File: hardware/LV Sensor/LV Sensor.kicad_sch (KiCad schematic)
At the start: 75 parts, among them J1 Conn_01x04_Pin, J2 Conn_01x02_Pin, J3 TH, J4 TH, J5 TH, J6 TH, SW1 SW_Push, U1 MSPM0G3507 RHB32, U10 DXTN80100CFGQ, U2 ISO1042BDW, U3 KA78M05_TO252, U4 KA78M05_TO252, U5 L78L33_SO8, U6 LM324BAIPWR, U7 HBDM60V600X, U8 LM324BAIPWR, U9 DXTN80100CFGQ

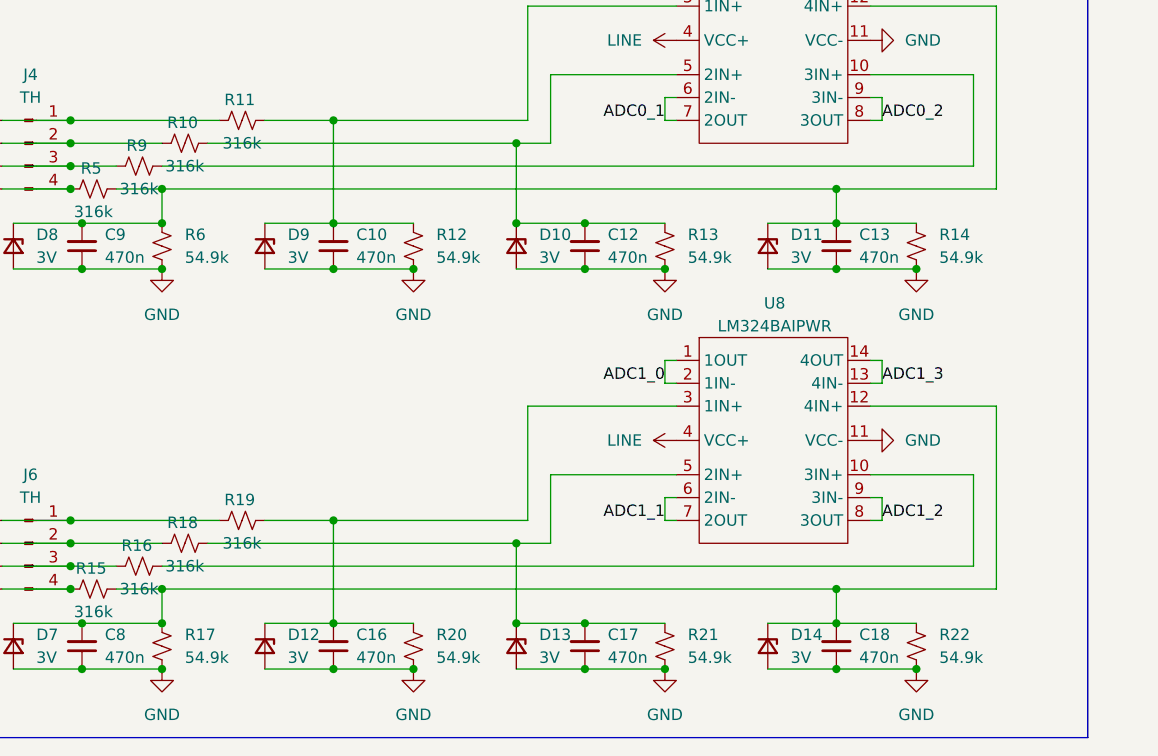
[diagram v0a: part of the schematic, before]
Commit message: miswired filter, also forgot about negative ranges
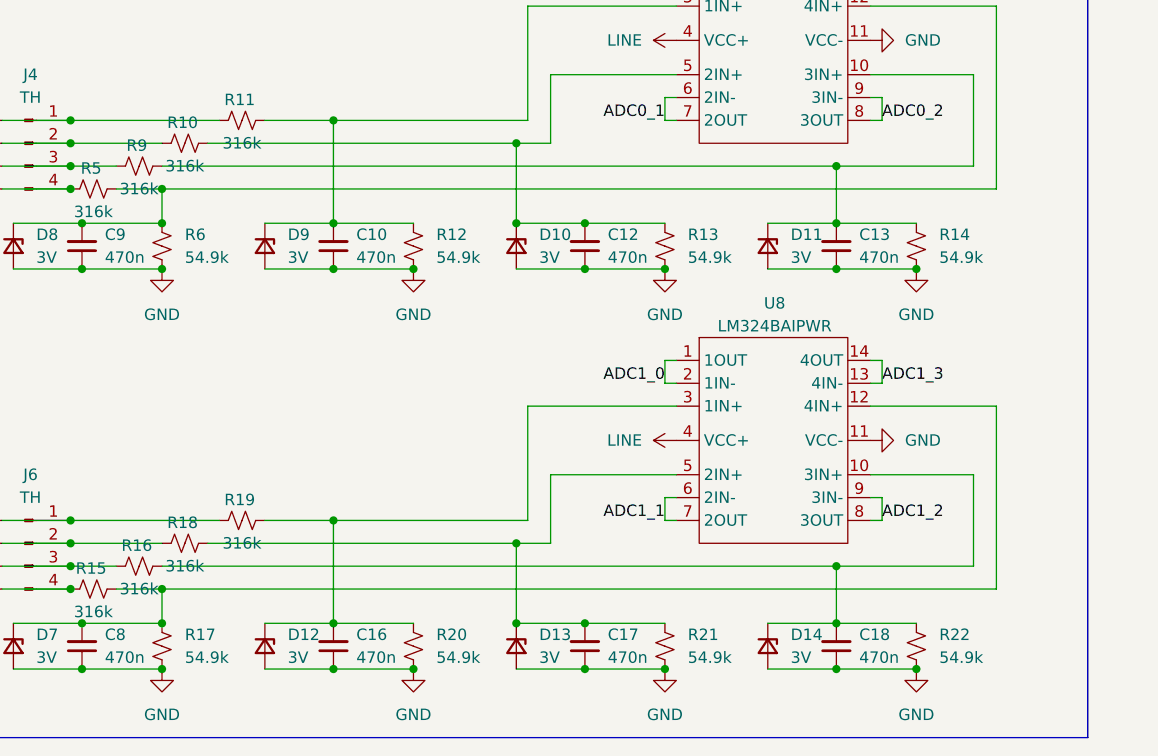
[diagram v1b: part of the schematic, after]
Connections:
- net at C9.2, D8.1 (K), R5.2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: no longer C13.2, D11.1 (K), R14.2
- net at C8.2, D7.1 (K), R15.2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: no longer C18.2, D14.1 (K), R22.2
- net at R9.2, U6.10 (3IN+): now also C13.2, D11.1 (K), R14.2
- net at R16.2, U8.10 (3IN+): now also C18.2, D14.1 (K), R22.2
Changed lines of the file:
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@@
-	)
-	(junction
-		(at 115.57 180.34)
-		(diameter 0)
-		(color 0 0 0 0)
 	)
 	(junction
@@
 	)
 	(junction
-		(at 115.57 135.89)
-		(diameter 0)
-		(color 0 0 0 0)
-	)
-	(junction
 		(at 106.68 86.36)
 		(diameter 0)
@@
 	)
 	(junction
+		(at 115.57 133.35)
+		(diameter 0)
+		(color 0 0 0 0)
+	)
+	(junction
 		(at 59.69 189.23)
 		(diameter 0)
@@
 	(junction
 		(at 87.63 41.91)
+		(diameter 0)
+		(color 0 0 0 0)
+	)
+	(junction
+		(at 115.57 177.8)
 		(diameter 0)
 		(color 0 0 0 0)
@@
 	(wire
 		(pts
-			(xy 115.57 135.89) (xy 133.35 135.89)
+			(xy 40.64 135.89) (xy 133.35 135.89)
 		)
 		(stroke
@@
 	(wire
 		(pts
+			(xy 115.57 177.8) (xy 115.57 184.15)
+		)
+		(stroke
+			(width 0)
+			(type default)
+		)
+	)
+	(wire
+		(pts
 			(xy 39.37 36.83) (xy 46.99 36.83)
 		)
@@
 	(wire
 		(pts
-			(xy 40.64 177.8) (xy 130.81 177.8)
+			(xy 40.64 177.8) (xy 115.57 177.8)
 		)
 		(stroke
@@
 	(wire
 		(pts
-			(xy 115.57 180.34) (xy 115.57 184.15)
-		)
-		(stroke
-			(width 0)
-			(type default)
-		)
-	)
-	(wire
-		(pts
 			(xy 120.65 154.94) (xy 119.38 154.94)
 		)
@@
 	(wire
 		(pts
-			(xy 40.64 133.35) (xy 130.81 133.35)
+			(xy 40.64 133.35) (xy 115.57 133.35)
 		)
 		(stroke
@@
 	(wire
 		(pts
+			(xy 115.57 133.35) (xy 115.57 139.7)
+		)
+		(stroke
+			(width 0)
+			(type default)
+		)
+	)
+	(wire
+		(pts
 			(xy 22.86 81.28) (xy 22.86 93.98)
 		)
@@
 	(wire
 		(pts
+			(xy 115.57 177.8) (xy 130.81 177.8)
+		)
+		(stroke
+			(width 0)
+			(type default)
+		)
+	)
+	(wire
+		(pts
 			(xy 69.85 49.53) (xy 80.01 49.53)
 		)
@@
 	(wire
 		(pts
+			(xy 115.57 133.35) (xy 130.81 133.35)
+		)
+		(stroke
+			(width 0)
+			(type default)
+		)
+	)
+	(wire
+		(pts
 			(xy 191.77 49.53) (xy 201.93 49.53)
 		)
@@
 	(wire
 		(pts
-			(xy 40.64 135.89) (xy 115.57 135.89)
-		)
-		(stroke
-			(width 0)
-			(type default)
-		)
-	)
-	(wire
-		(pts
 			(xy 22.86 135.89) (xy 30.48 135.89)
 		)
@@
 	(wire
 		(pts
-			(xy 40.64 180.34) (xy 115.57 180.34)
+			(xy 40.64 180.34) (xy 133.35 180.34)
 		)
 		(stroke
@@
 	(wire
 		(pts
-			(xy 115.57 135.89) (xy 115.57 139.7)
-		)
-		(stroke
-			(width 0)
-			(type default)
-		)
-	)
-	(wire
-		(pts
 			(xy 133.35 41.91) (xy 132.08 41.91)
 		)
@@
 		)
 		(stroke
-			(width 0)
-			(type default)
-		)
-	)
-	(wire
-		(pts
-			(xy 115.57 180.34) (xy 133.35 180.34)
-		)
-		(stroke

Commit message: asd
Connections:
- net LED_GREEN: no longer U1.27 (PA23_VREF+)
- net LED_RED_N: no longer U1.26 (PA22_A0_7)
- no-connect marks 8 -> 6
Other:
- note added: "TODO. somehow support negative voltage range, like 2 inputs that support it, the rest can get shoved thoruhg the ADC's. probably a external adc IC"
- moved on the sheet: D5, D6, R3, R4, U7

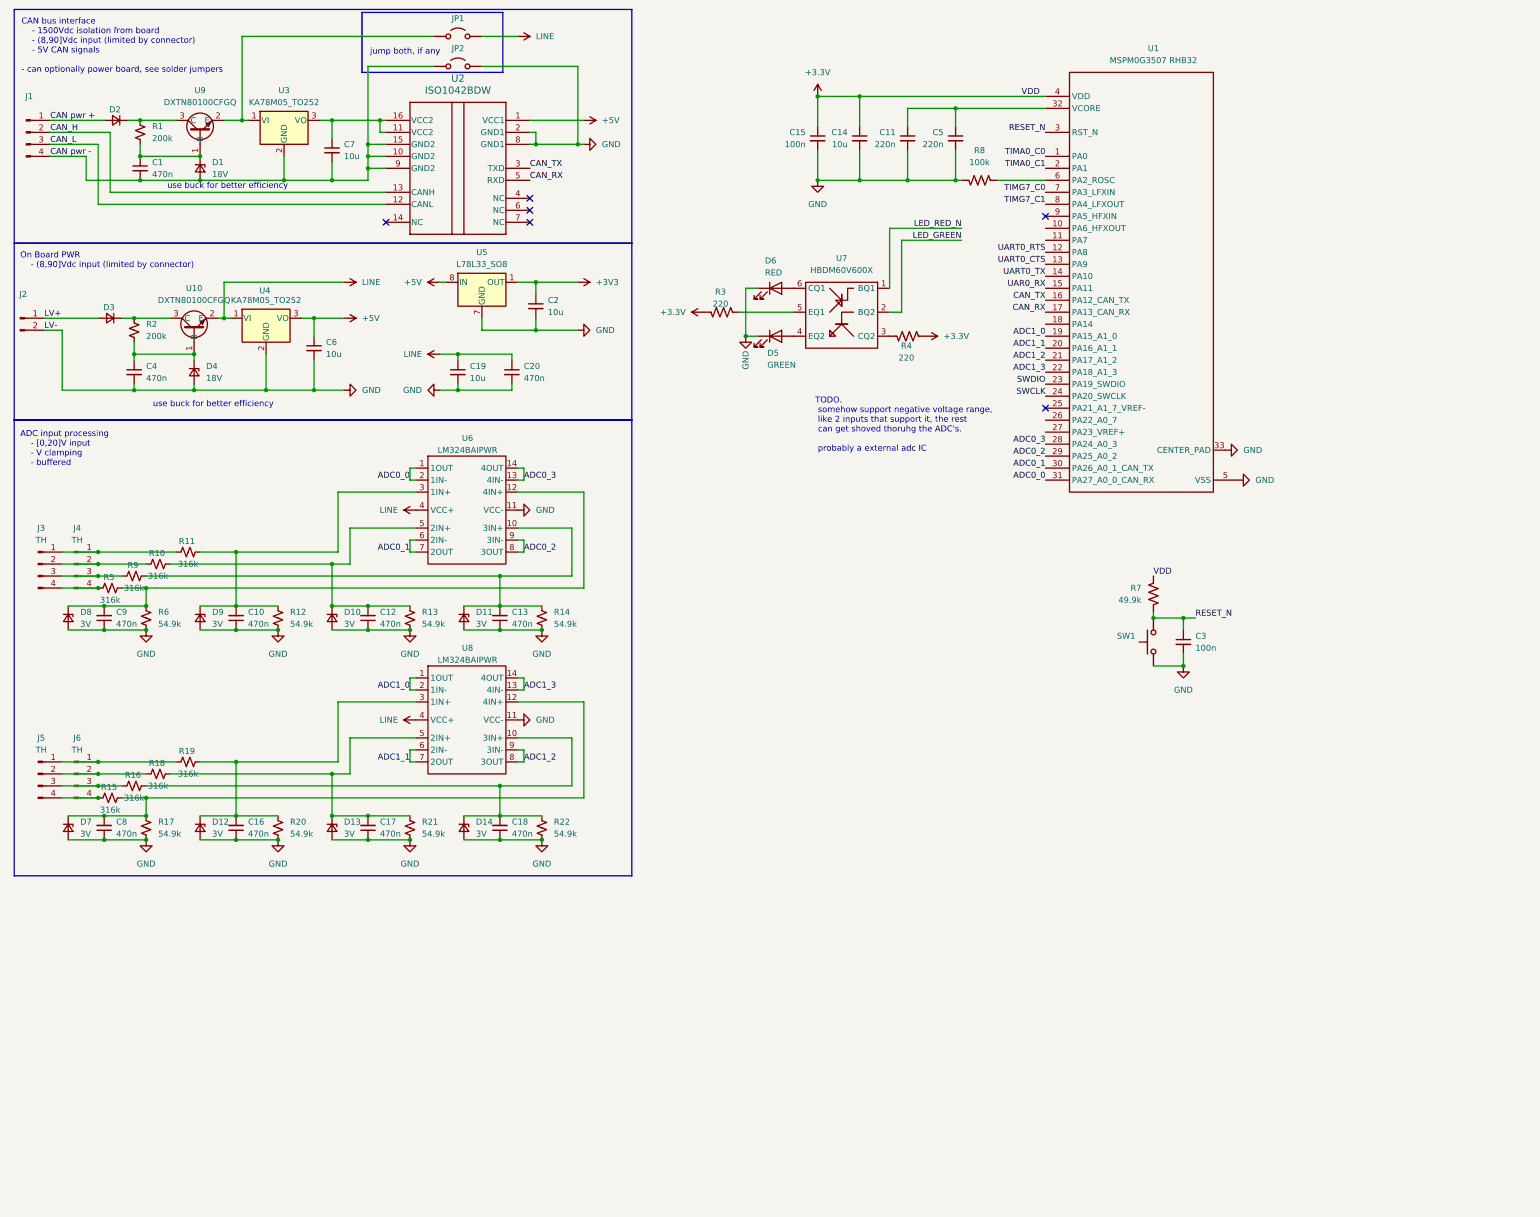
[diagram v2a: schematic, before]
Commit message: why was the can CCS project in the kicad folder
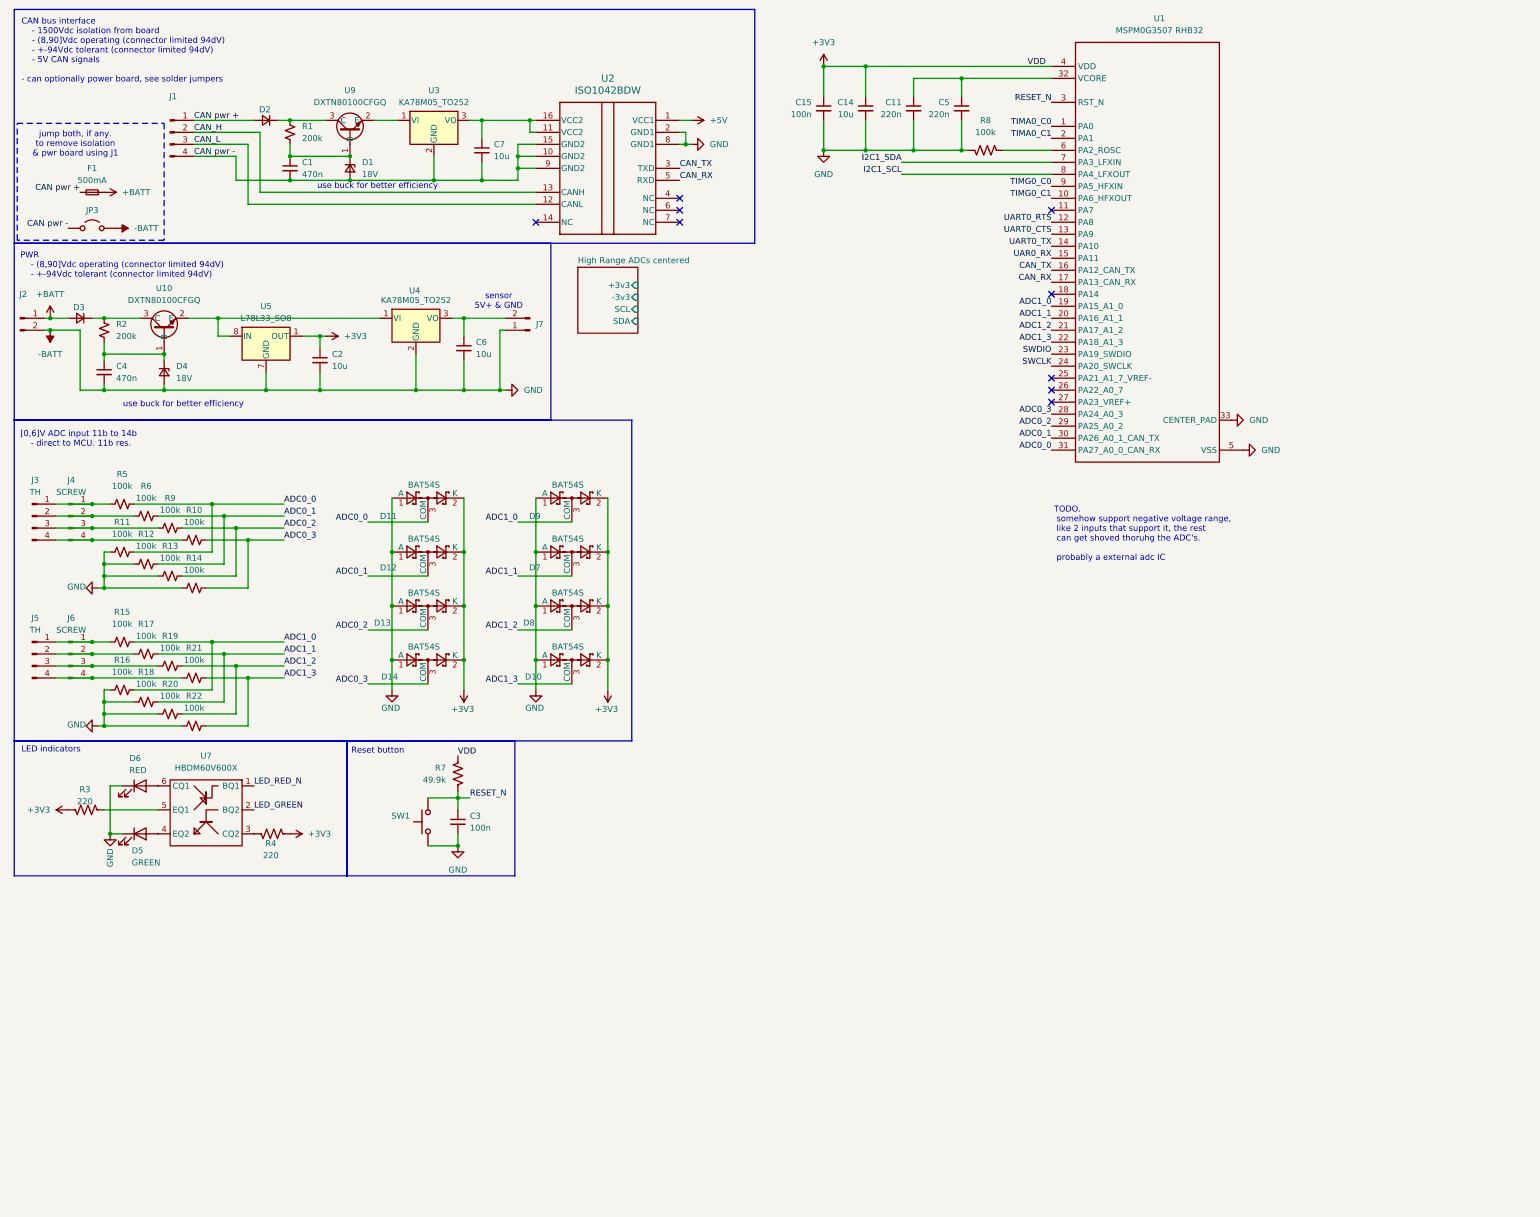
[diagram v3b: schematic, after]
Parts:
- removed C10, C12, C13, C16, C17, C18, C20, C8, C9: 470n, Capacitor_SMD:C_0805_2012Metric_Pad1.18x1.45mm_HandSolder, symbol Device:C_Small
- removed C19: 10u, Capacitor_SMD:C_1206_3216Metric_Pad1.33x1.80mm_HandSolder, symbol Device:C_Small
- removed D10, D11, D12, D13, D14, D7, D8, D9: 3V, Diode_SMD:D_SOD-123F, symbol Device:D_Zener_Small
- removed JP1, JP2: Jumper_2_Open, Jumper:Jumper_Harwin_S1621_P10.9mm, symbol Jumper:Jumper_2_Open
- removed U6, U8: LM324BAIPWR, Package_SO:TSSOP-14_4.4x5mm_P0.65mm, symbol zzLocalLibrary:LM324BAIPWR
- added D10, D11, D12, D13, D14, D7, D8, D9: BAT54S, Package_TO_SOT_SMD:SOT-23-3, symbol Diode:BAT54S
- added F1: 500mA, symbol Device:Fuse_Small
- added J7: Conn_01x02_Pin, Connector_Molex:Molex_Mini-Fit_Jr_5569-02A1_2x01_P4.20mm_Horizontal, symbol Connector:Conn_01x02_Pin
- added JP3: Jumper_2_Open, Jumper:Jumper_Harwin_S1621_P10.9mm, symbol Jumper:Jumper_2_Open
- J3, J5: footprint Diode_THT:Diode_Bridge_19.0x3.5x10.0mm_P5.0mm -> Connector_PinHeader_2.54mm:PinHeader_1x04_P2.54mm_Vertical
- J4, J6: value TH -> SCREW
- R10, R11, R15, R16, R18, R19, R5, R9: value 316k -> 100k; footprint Resistor_SMD:R_0805_2012Metric_Pad1.20x1.40mm_HandSolder -> (none); mouser https://www.mouser.com/ProductDetail/Panasonic/ERA-6AEB3163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 -> https://www.mouser.com/ProductDetail/YAGEO/RC1206FR-07100KL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; unit x1 0.054 -> 0.10; unit x10 0.1 -> 0.016
- R12, R13, R14, R17, R20, R21, R22, R6: value 54.9k -> 100k; footprint Resistor_SMD:R_0805_2012Metric_Pad1.20x1.40mm_HandSolder -> (none); mouser https://www.mouser.com/ProductDetail/Panasonic/ERA-3AEB5492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 -> https://www.mouser.com/ProductDetail/YAGEO/RC1206FR-07100KL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; unit x1 0.054 -> 0.10; unit x10 0.1 -> 0.016
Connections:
- net +3.3V is gone; now on net +3V3: C14.1, C15.1, R3.2, R4.2, R7.1, U1.4 (VDD)
- net +3V3: now also D10.2 (K), D11.2 (K), D12.2 (K), D13.2 (K), D14.2 (K), D7.2 (K), D8.2 (K), D9.2 (K)
- net +5V: no longer C6.1, U4.3 (VO), U5.8 (IN)
- net ADC0_0: now also R11.2, R5.2, D11.3 (COM)
- net ADC0_1: now also R12.2, R6.2, D12.3 (COM)
- net ADC0_2: now also R13.2, R9.2, D13.3 (COM)
- net ADC0_3: now also R10.2, R14.2, D14.3 (COM)
- net ADC1_0: now also R15.2, R16.2, D9.3 (COM)
- net ADC1_1: now also R17.2, R18.2, D7.3 (COM)
- net ADC1_2: now also R19.2, R20.2, D8.3 (COM)
- net ADC1_3: now also R21.2, R22.2, D10.3 (COM)
- net CAN pwr +: now also F1.2
- net CAN pwr -: now also JP3.1 (A)
- net at J5.2 (Pin_2), J6.2 (Pin_2): now also R17.1; no longer R18.1
- net at J3.1 (Pin_1), J4.1 (Pin_1): now also R5.1; no longer R11.1
- net at J3.2 (Pin_2), J4.2 (Pin_2): now also R6.1; no longer R10.1
- net at J3.4 (Pin_4), J4.4 (Pin_4): now also R10.1; no longer R5.1
- net TIMG0_C1: now reaches U1.10 (PA6_HFXOUT)
- net TIMG0_C0: now reaches U1.9 (PA5_HFXIN)
- net at J5.3 (Pin_3), J6.3 (Pin_3): now also R19.1; no longer R16.1
- net at J5.4 (Pin_4), J6.4 (Pin_4): now also R21.1; no longer R15.1
- net at J5.1 (Pin_1), J6.1 (Pin_1): now also R15.1; no longer R19.1
- net GND renamed -BATT
- net -BATT: now also R11.1, R16.1, R18.1, D10.1 (A), D11.1 (A), D12.1 (A), D13.1 (A), D14.1 (A), D7.1 (A), D8.1 (A), D9.1 (A), J7.1 (Pin_1), JP3.2 (B); no longer R17.1, R21.1, R6.1
- net LINE: no longer names the net of U10.2 (E), U4.1 (VI)
- net LINE: now also U5.8 (IN)
- net LV+ renamed +BATT
- net +BATT: now also F1.1
- net TIMG7_C0 renamed I2C1_SDA
- net TIMG7_C1 renamed I2C1_SCL
- new net: C6.1, J7.2 (Pin_2), U4.3 (VO)
- no-connect marks 6 -> 9
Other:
- added sheet High Range ADCs centered (High Range ADCs centered.kicad_sch)
- note added: "CAN bus interface - 1500Vdc isolation from board - (8,90]Vdc operating (connector limited 94dV) - +-94Vdc tolerant (connector limited 94dV) - 5V CAN signals - can optionally power board, see solder jumpers"
- note added: "LED indicators"
- note added: "PWR - (8,90]Vdc operating (connector limited 94dV) - +-94Vdc tolerant (connector limited 94dV)"
- note added: "Reset button"
- note added: "[0,6]V ADC input 11b to 14b - direct to MCU. 11b res."
- note added: "jump both, if any. to remove isolation & pwr board using J1"
- note added: "sensor 5V+ & GND"
- note removed: "ADC input processing - [0,20]V input - V clamping - buffered"
- note removed: "CAN bus interface - 1500Vdc isolation from board - (8,90]Vdc input (limited by connector) - 5V CAN signals - can optionally power board, see solder jumpers"
- note removed: "On Board PWR - (8,90]Vdc input (limited by connector)"
- note removed: "jump both, if any"
- moved on the sheet: C1, C11, C14, C15, C2, C3, C4, C5, C6, C7, D1, D2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
